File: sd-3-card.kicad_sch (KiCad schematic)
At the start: 22 parts, among them J2 1140084168, Q1 BSS123, Q2 AO3401A, U5 NVT4858HKZ, U6 TPS2116DRLR

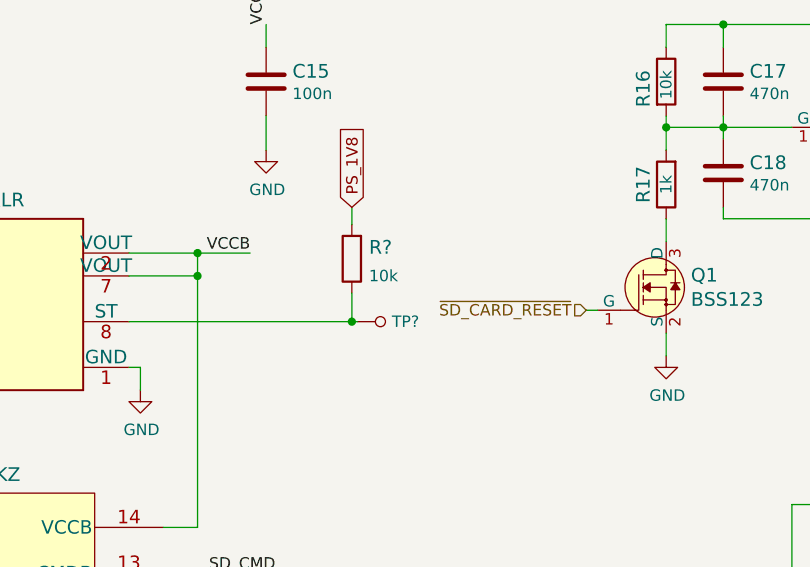
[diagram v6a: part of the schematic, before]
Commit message: Add decoupling to cammera and DP connector, schematic cleanup
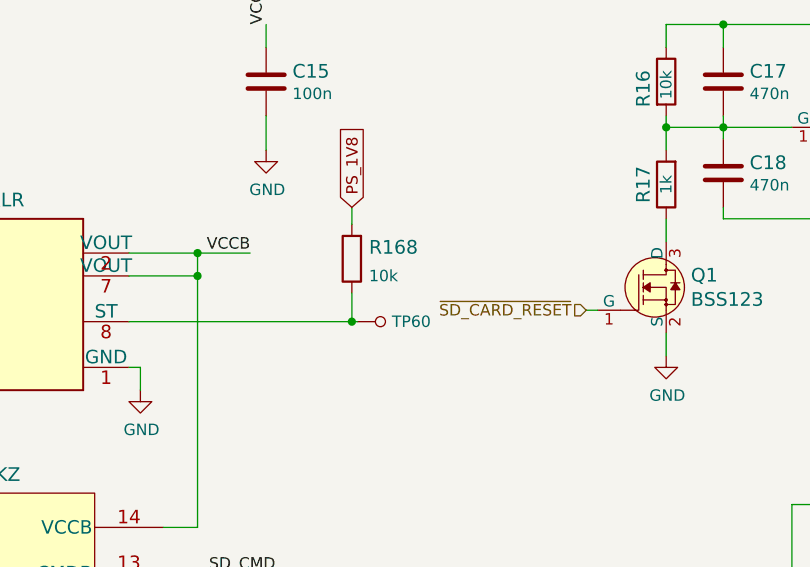
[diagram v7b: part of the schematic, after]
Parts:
- gave numbers to parts that had none: 2
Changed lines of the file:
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@@
   (symbol (lib_id "antmicroResistors0402:R_10k_0402") (at 160.655 84.455 90) (unit 1)
     (in_bom yes) (on_board yes) (fields_autoplaced)
-    (property "Reference" "R?" (id 0) (at 162.56 83.185 90)
+    (property "Reference" "R168" (id 0) (at 162.56 83.185 90)
       (effects (font (size 1.524 1.524)) (justify right))
     )
@@
   (symbol (lib_id "antmicroTestPoints:TP_SMD_0_75MM") (at 163.83 91.44 90) (unit 1)
     (in_bom yes) (on_board yes) (fields_autoplaced)
-    (property "Reference" "TP?" (id 0) (at 165.1 91.4399 90)
+    (property "Reference" "TP60" (id 0) (at 165.1 91.4399 90)
       (effects (font (size 1.27 1.27)) (justify right))
     )
